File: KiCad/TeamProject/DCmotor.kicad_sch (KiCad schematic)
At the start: 15 parts, among them M1 Right_Motor_DC, M2 Left_Motor_DC, U1 L293

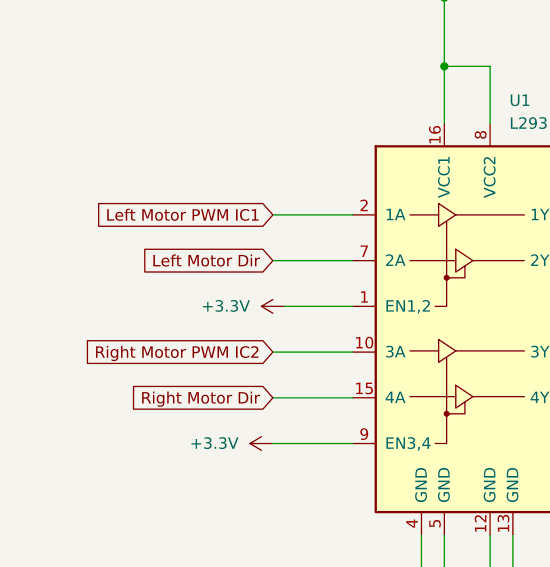
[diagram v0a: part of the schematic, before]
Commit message: change Pin of SPI
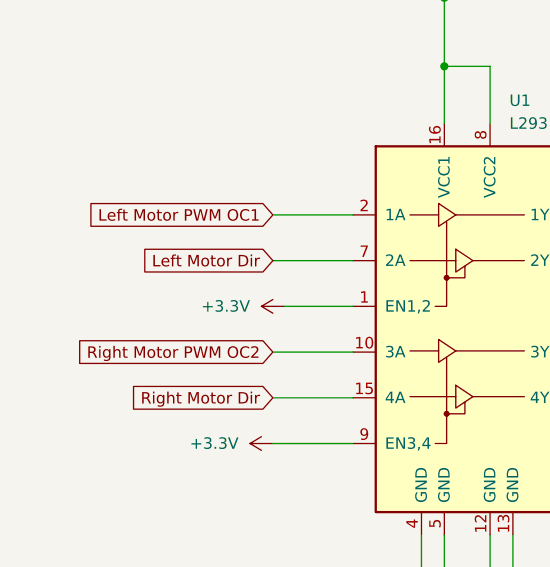
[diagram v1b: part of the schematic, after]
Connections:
- net Left Motor PWM IC1 renamed Left Motor PWM OC1
- net Right Motor PWM IC2 renamed Right Motor PWM OC2
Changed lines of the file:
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@@
 		)
 	)
-	(global_label "Right Motor PWM IC2"
+	(global_label "Right Motor PWM OC2"
 		(shape input)
 		(at 53.34 92.71 180)
@@
 		)
 		(property "Intersheetrefs" "${INTERSHEET_REFS}"
-			(at 30.0351 92.71 0)
+			(at 29.3094 92.71 0)
 			(effects
 				(font
@@
 		)
 	)
-	(global_label "Left Motor PWM IC1"
+	(global_label "Left Motor PWM OC1"
 		(shape input)
 		(at 53.34 77.47 180)
@@
 		)
 		(property "Intersheetrefs" "${INTERSHEET_REFS}"
-			(at 31.3655 77.47 0)
+			(at 30.6398 77.47 0)
 			(effects
 				(font

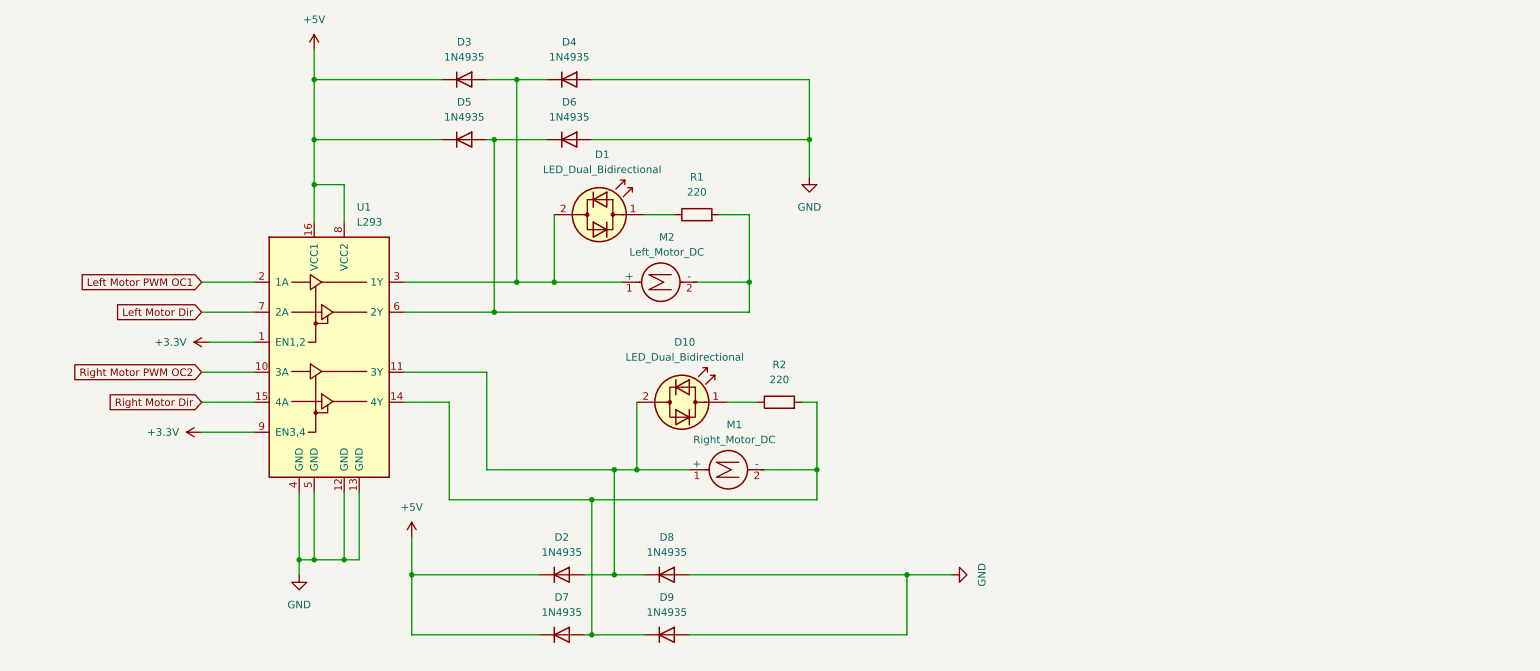
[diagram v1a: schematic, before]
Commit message: Updated schematics to more closely match final
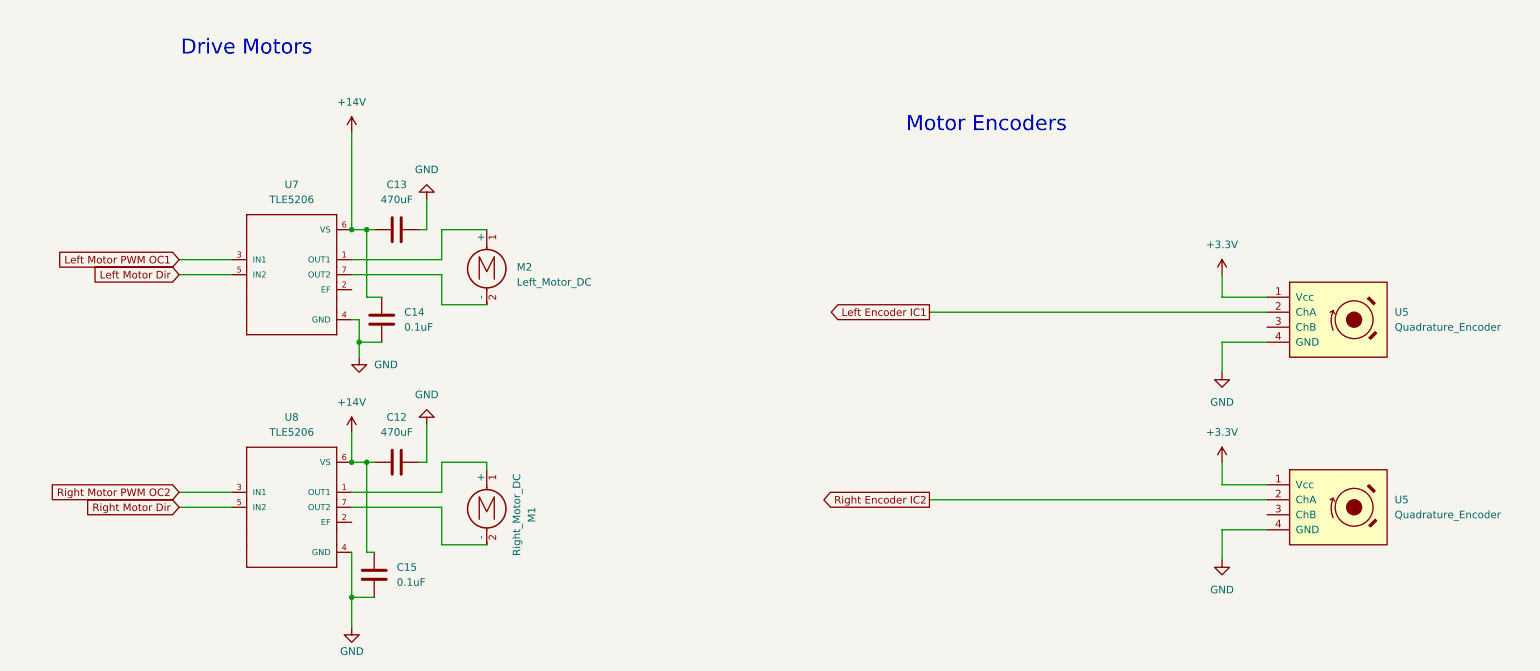
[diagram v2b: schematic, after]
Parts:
- removed D1, D10: LED_Dual_Bidirectional, symbol Device:LED_Dual_Bidirectional
- removed D2, D3, D4, D5, D6, D7, D8, D9: 1N4935, Diode_THT:D_DO-41_SOD81_P10.16mm_Horizontal, symbol Diode:1N4007
- removed R1, R2: 220, symbol Device:R
- removed U1: L293, Package_DIP:DIP-16_W7.62mm, symbol Driver_Motor:L293
- added C12, C13: 470uF, symbol ME218:Cap
- added C14, C15: 0.1uF, symbol ME218:Cap
- added U5 (x2): Quadrature_Encoder, symbol ME218_BaseLib:Quadrature_Encoder
- added U7, U8: TLE5206, TLE5206-2G:DPAK127P1500X440-8N, symbol TLE5206:TLE5206-2G
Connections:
- net +3.3V: now also U5.1 (Vcc), U5.1 (Vcc)
- net GND: now also C12.2, C13.2, C14.2, C15.2, U5.4 (GND), U5.4 (GND), U7.4 (GND), U8.4 (GND)
- net Left Motor Dir: now also U7.5 (IN2)
- net Left Motor PWM OC1: now also U7.3 (IN1)
- net Right Motor Dir: now also U8.5 (IN2)
- net Right Motor PWM OC2: now also U8.3 (IN1)
- net at M1.2 (-): now also U8.7 (OUT2)
- net at M1.1 (+): now also U8.1 (OUT1)
- net at M2.2 (-): now also U7.7 (OUT2)
- net at M2.1 (+): now also U7.1 (OUT1)
- new net +14V: C12.1, C13.1, C14.1, C15.1, U7.6 (VS), U8.6 (VS)
- new net Left Encoder IC1: U5.2 (ChA)
- new net Right Encoder IC2: U5.2 (ChA)
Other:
- note added: "Drive Motors"
- note added: "Motor Encoders"
- moved on the sheet: M1, M2
